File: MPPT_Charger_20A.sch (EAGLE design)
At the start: 113 parts, among them IC1 LM358D, Q1 IRFR3607, Q2 IRFR3607, Q3 IRFR3607, Q5 IRFR3607, Q7 ZXMP10A13FTA, T1 MMBT3904, U1 SN65HVD230, U2 INA199A1DCKR, U3 LM5101A, U4 MCP16311, U5 MIC5225, U6 STM32F072CB, U7 INA199A1DCKR, Y1 8MHz

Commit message: Updated revision with 20A charge current
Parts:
- removed BATTERY: MKDS_5/2-9,52, resolut:MKDS_5/2-9,52
- removed H1, H2, H3, H4: MOUNT-HOLE2.8, holes:MOUNT-HOLE2.8
- removed IC1: LM358D, linear:LM358D
- removed K1: (no value), Input-Output_Connectors_rev15d:629105150521
- removed LED3: (no value), SparkFun-LED:LED3MM
- removed LED4, LED5, LED6: (no value), SparkFun-LED:LED0603
- removed Q5: IRFR3607, LibreSolar:MOSFET_N_DPAK
- removed Q7: ZXMP10A13FTA, transistor-small-signal:BSS84
- removed R48: 2.2k, rcl:R-EU_R0603
- removed S2: (no value), LibreSolar:SWITCH-DPDT_CK_JS
- removed SWD: CORTEX_DEBUGSMD, LibreSolar:CORTEX_DEBUGSMD
- removed X1: (no value), crystal:CRYSTALMM20SS
- added BAT: MKDS_5/2-9,52, resolut:MKDS_5/2-9,52
- added C33, C36: 2.2µ, LibreSolar:CAPACITOR_0603
- added C34: 100n, LibreSolar:CAPACITOR_0603
- added C35: 1µ, LibreSolar:CAPACITOR_0603
- added C37: 10µ, rcl:C-EUC0805
- added C38: 100p, LibreSolar:CAPACITOR_0603
- added C39: DNP, LibreSolar:CAPACITOR_0603
- added D11: 1N4148W-7-F, SparkFun-DiscreteSemi:DIODESOD123
- added D12: SS16FP, resolut:SCHOTTKY-DIODEPOWERDI123
- added D6, D8: (no value), SparkFun-LED:LED0603
- added I2C: (no value), SparkFun-Connectors:M04PTH
- added IC2: LM4040CYM3-2.5, texas:LM4041A12DBZ
- added JP3: RJ45, SparkFun-Connectors:RJ45-8PTH
- added NTC1, NTC2: NTC10k, LibreSolar:THERMISTOR_0603
- added Q4: CSD18540Q5B, LibreSolar:MOSFET_N_5X6
- added R34: 100k, LibreSolar:RESISTOR_R0603
- added R35, R36, R41: 2.2k, LibreSolar:RESISTOR_R0603
- added R37: 10k, LibreSolar:RESISTOR_R0603
- added R39, R40: 1M, LibreSolar:RESISTOR_R0603
- added R42, R43: 330, LibreSolar:RESISTOR_R0603
- added RESET: (no value), EAGLE-TACT_SWITCHES-rev16e:430182050816
- added T2: MMBT3904, transistor:MMBT3904LT1-NPN-SOT23-BEC
- added U$1: LIBRESOLAR_LOGO, LibreSolar:LIBRESOLAR_LOGO
- added USB: USB_MICRO_B, LibreSolar:USB_MICRO_B
- added Y2: ABS25-32.768KHZ-T, crystal:CRYSTALMM20SS
- C1: value 470µ -> 1000µ; device rcl:CPOL-EUE5-13 -> rcl:CPOL-EUE7.5-16; MPN EEUFR1J471B -> EEUFC1J102; OC_FARNELL 2079308 -> 9692576
- C10: value 4.7µ -> 100n; device rcl:C-EUC1210 -> LibreSolar:CAPACITOR_0603; MPN GRM31CR71H475KA12L -> GRM188R71H104KA93D; OC_FARNELL 1735545 -> 8820023
- C11: value 22µ -> 100n; device rcl:C-EUC1210 -> LibreSolar:CAPACITOR_0603; MF MULTICOMP -> MURATA; MPN MC1210B226M160CT -> GRM188R71H104KA93D; OC_FARNELL 2320948 -> 8820023
- C12, C23: value 100n -> 1µ; device rcl:C-EUC0603 -> LibreSolar:CAPACITOR_0603; MF MURATA -> AVX; MPN GRM188R71H104KA93D -> 08055C104KAT2A; OC_FARNELL 8820023 -> 499687
- C13: value 0 -> 100n; device rcl:C-EUC0603 -> LibreSolar:CAPACITOR_0603; MF AVX -> MURATA; MPN 08055C104KAT2A -> GRM188R71H104KA93D; OC_FARNELL 499687 -> 8820023
- C14, C15: value 100n -> 10µ; device rcl:C-EUC0603 -> rcl:C-EUC0805; MPN GRM188R71H104KA93D -> GRM21BR61E106KA73L; OC_FARNELL 8820023 -> 1735530
- C16, C17, C19, C26, C30: device rcl:C-EUC0603 -> LibreSolar:CAPACITOR_0603
- C18: value 470µ -> 100n; device rcl:CPOL-EUE5-13 -> LibreSolar:CAPACITOR_0603; MF PANASONIC ELECTRONIC COMPONENTS -> MURATA; MPN EEUFR1J471B -> GRM188R71H104KA93D; OC_FARNELL 2079308 -> 8820023
- C2: value 1µ -> 1000µ; device rcl:C-EUC0805 -> rcl:CPOL-EUE7.5-16; MF TDK -> PANASONIC ELECTRONIC COMPONENTS; MPN C2012X7S2A105M125AB -> EEUFC1J102; OC_FARNELL 2528783 -> 9692576
- C20: value 100n -> 1µ; device rcl:C-EUC0603 -> rcl:C-EUC0805; MF MURATA -> (none); MPN GRM188R71H104KA93D -> (none); OC_FARNELL 8820023 -> unknown
- C21: value 100n -> 4.7µ; device rcl:C-EUC0603 -> rcl:C-EUC1210; MPN GRM188R71H104KA93D -> GRM31CR71H475KA12L; OC_FARNELL 8820023 -> 1735545
- C22: value 100n -> 10µ; device rcl:C-EUC0603 -> rcl:C-EUC0805; MF AVX -> MURATA; MPN 06035C104KAT2A -> GRM21BR61E106KA73L; OC_FARNELL 1301804 -> 1735530
- C24: value 100n -> 2.2µ; device rcl:C-EUC0603 -> LibreSolar:CAPACITOR_0603; MF MURATA -> AVX; MPN GRM188R71H104KA93D -> 0805YC475KAT2A; OC_FARNELL 8820023 -> 1657937
- C25: value 2.2µ -> 100n; device rcl:C-EUC0603 -> LibreSolar:CAPACITOR_0603; MF AVX -> MURATA; MPN 0805YC475KAT2A -> GRM188R71H104KA93D; OC_FARNELL 1657937 -> 8820023
- C27: value 2.2µ -> 12.5p; device rcl:C-EUC0603 -> LibreSolar:CAPACITOR_0603; MF AVX -> MURATA; MPN 0805YC475KAT2A -> GRM188R71H104KA93D; OC_FARNELL 1657937 -> 8820023
- C28: value 270µ -> 12.5p; device rcl:CPOL-EUE5-10.5 -> LibreSolar:CAPACITOR_0603; MF PANASONIC ELECTRONIC COMPONENTS -> MURATA; MPN EEUFR1J271LB -> GRM188R71H104KA93D; OC_FARNELL 2079304 -> 8820023
- C29, C9: value 1µ -> 100n; device rcl:C-EUC0603 -> LibreSolar:CAPACITOR_0603; MF AVX -> MURATA; MPN 08055C104KAT2A -> GRM188R71H104KA93D; OC_FARNELL 499687 -> 8820023
- C3: value 1µ -> 2.2µ; device rcl:C-EUC0805 -> rcl:C-EUC1210; MF TDK -> (none); MPN C2012X7S2A105M125AB -> (none); OC_FARNELL 2528783 -> unknown
- C31, C32: value 12.5p -> 100n; device rcl:C-EUC0603 -> LibreSolar:CAPACITOR_0603
- C4: value 680µ -> 1µ; device rcl:CPOL-EUE5-10.5 -> LibreSolar:CAPACITOR_0805; MF PANASONIC ELECTRONIC COMPONENTS -> (none); MPN EEUFR1V681LB -> (none); OC_FARNELL 1800669 -> unknown
- C5: value 100n -> 1µ; device rcl:C-EUC0603 -> LibreSolar:CAPACITOR_0805; MF MURATA -> (none); MPN GRM188R71H104KA93D -> (none); OC_FARNELL 8820023 -> unknown
- C6: value 1µ -> 1n; device rcl:C-EUC0603 -> rcl:C-EUC0805; MF AVX -> MULTICOMP; MPN 08055C104KAT2A -> MCU0805C102JCT; OC_FARNELL 499687 -> 9406212
- C7: value 1n -> 680µ; device rcl:C-EUC0805 -> rcl:CPOL-EUE5-10.5; MF MULTICOMP -> PANASONIC ELECTRONIC COMPONENTS; MPN MCU0805C102JCT -> EEUFR1V681LB; OC_FARNELL 9406212 -> 1800669
- C8: value 100n -> 680µ; device rcl:C-EUC0603 -> rcl:CPOL-EUE5-10.5; MF MURATA -> PANASONIC ELECTRONIC COMPONENTS; MPN GRM188R71H104KA93D -> EEUFR1V681LB; OC_FARNELL 8820023 -> 1800669
- D2: value 1N4148W-7-F -> SS16FP; device SparkFun-DiscreteSemi:DIODESOD123 -> resolut:SCHOTTKY-DIODEPOWERDI123; MF MULTICOMP -> DIODES INC.; MPN 1N4148W -> DFLS1100-7; OC_FARNELL 1621821 -> 1713889
- D3: value PESD2CAN -> NUP2105L
- D4: value 1N4148W-7-F -> (none); device SparkFun-DiscreteSemi:DIODESOD123 -> LibreSolar:USBLC6-2; MF MULTICOMP -> (none); MPN 1N4148W -> (none); OC_FARNELL 1621821 -> (none)
- F1: value 12A -> 25A; device LibreSolar:FUSE_BLADE_STD -> LibreSolar:FUSE_KEYSTONE-3557-2; MPN 3522-2 -> 3557-2; OC_FARNELL 1608220 -> 2292904
- JP1: value RJ45 -> CORTEX_DEBUGSMD; device SparkFun-Connectors:RJ45-8PTH -> LibreSolar:CORTEX_DEBUGSMD; MF AMPHENOL COMMERCIAL PRODUCTS -> (none); MPN RJHSE-5080 -> (none); OC_FARNELL 1860577 -> unknown
- JP4, UEXT: OC_FARNELL (none) -> unknown
- L1: device PowerMagnetics:WE-HCF_2818_7443643300 -> LibreSolar:L-FERYSTER-DTMSS-27/0,033/20-H; MF COILCRAFT -> (none); MPN SER2918H-223KL -> (none); OC_FARNELL 2288918 -> unknown
- L2: value 47µH -> 4.7uH; device PowerMagnetics:WE-TPC_4818/4828 -> rcl:L-EUL2012C; MPN 744043470 -> 74476404; OC_FARNELL 1890607 -> 2471630
- L3: value 22µ -> 22µH; device LibreSolar:L-BOURNS2300-H -> PowerMagnetics:WE-TPC_4818/4828; MF BOURNS -> WURTH ELEKTRONIK; MPN 2305-V-RC -> 744043470; OC_FARNELL 1929755 -> 1890607
- L4: value WE-SD_744710215 -> (none); device PowerMagnetics:WE-SD_744710215 -> EAGLE-EMC_COMPONENTS-rev16f:WE-CBA_0603(WB/HS); MF WURTH ELEKTRONIK -> (none); MPN 744710215 -> (none); OC_FARNELL 1635814 -> unknown
- LOAD, SOLAR: MF (none) -> PHOENIX CONTACT; MPN (none) -> 1714971; OC_FARNELL unknown -> 3704701
- Q1, Q2, Q3: value IRFR3607 -> CSD18540Q5B; device LibreSolar:MOSFET_N_DPAK -> LibreSolar:MOSFET_N_5X6; MF INTERNATIONAL RECTIFIER -> TEXAS INSTRUMENTS; MPN IRFR3607TRPBF -> CSD18540Q5BT; OC_FARNELL 2101420 -> 2447870
- R1, R3: value 4.7 -> 3.3; device rcl:R-EU_R0805 -> LibreSolar:RESISTOR_R0805
- R10: value 120k -> 3.3; device rcl:R-EU_R0603 -> LibreSolar:RESISTOR_R0805; MF YAGEO (PHYCOMP) -> BOURNS; MPN RC0603FR-07120KL -> CR0805-FX-1001ELF; OC_FARNELL 9238735 -> 2008380
- R11: value 10k -> 1k; device rcl:R-EU_R0603 -> LibreSolar:RESISTOR_R0603; MPN RC0603FR-0710KL -> RC0603FR-071KL.; OC_FARNELL 9238603 -> 9238484
- R12: value 150k -> 2.2k; device rcl:R-EU_R0603 -> LibreSolar:RESISTOR_R0603; MPN RC0603FR-07150KL -> RC0603FR-071KL.; OC_FARNELL 9238743 -> 9238484
- R13: value 6.8k -> 2.2k; device rcl:R-EU_R0603 -> LibreSolar:RESISTOR_R0603; MPN RC0603FR-076K8L -> RC0603FR-071KL.; OC_FARNELL 9238581 -> 9238484
- R14: value 4.7 -> 150k; device rcl:R-EU_R1206 -> LibreSolar:RESISTOR_R0603; MPN RC1206FR-074R7L -> RC0603FR-071KL.; OC_FARNELL 9236600 -> 9238484
- R15: value 330 -> 150k; device rcl:R-EU_R0603 -> LibreSolar:RESISTOR_R0603; MPN RC0603FR-07330RL -> RC0603FR-071KL.; OC_FARNELL 9238425 -> 9238484
- R16, R29, R30: value 1k -> 10k; device rcl:R-EU_R0603 -> LibreSolar:RESISTOR_R0603; MPN RC0603FR-071KL. -> RC0603FR-0710KL; OC_FARNELL 9238484 -> 9238603
- R17: value 1k -> 2m; device rcl:R-EU_R0603 -> rcl:R-EU_R2512; MF YAGEO (PHYCOMP) -> BOURNS; MPN RC0603FR-071KL. -> CRF2512-FX-R005ELF; OC_FARNELL 9238484 -> 2008327
- R18, R19: value 10k -> 2.2k; device rcl:R-EU_R0603 -> LibreSolar:RESISTOR_R0603; MPN RC0603FR-0710KL -> RC0603FR-071KL.; OC_FARNELL 9238603 -> 9238484
- R2: value 4.7 -> 1M; device rcl:R-EU_R0805 -> LibreSolar:RESISTOR_R0603; MF BOURNS -> YAGEO (PHYCOMP); MPN CR0805-FX-1001ELF -> RC0603FR-071ML; OC_FARNELL 2008380 -> 9238840
- R20: value 33k -> 1k; device rcl:R-EU_R0603 -> LibreSolar:RESISTOR_R0603; MPN RC0603FR-0733KL -> RC0603FR-071KL.; OC_FARNELL 9238662 -> 9238484
- R21: value 10k -> 150k; device rcl:R-EU_R0603 -> LibreSolar:RESISTOR_R0603; MPN RC0603FR-0710KL -> RC0603FR-071KL.; OC_FARNELL 9238603 -> 9238484
- R22: value 2.2k -> 150k; device rcl:R-EU_R0603 -> LibreSolar:RESISTOR_R0603; MPN RC0603FR-072K2L. -> RC0603FR-071KL.; OC_FARNELL 9238522 -> 9238484
- R23: value 2.2k -> 10k; MPN RC0603FR-072K2L. -> RC0603FR-0710KL; OC_FARNELL 9238522 -> 9238603
- R24: value 330 -> 100k; device rcl:R-EU_R0603 -> LibreSolar:RESISTOR_R0603; MPN RC0603FR-07330RL -> RC0603FR-07150KL; OC_FARNELL 9238425 -> 9238743
- R25: value 120 -> 100k; device rcl:R-EU_R1206 -> LibreSolar:RESISTOR_R0603; MF WELWYN -> YAGEO (PHYCOMP); MPN WCR0805-120RFI -> RC0603FR-071KL.; OC_FARNELL 1100308 -> 9238484
- R26: value 0R -> 5.6k; device rcl:R-EU_R0603 -> LibreSolar:RESISTOR_R0603; MF PANASONIC ELECTRONIC COMPONENTS -> YAGEO (PHYCOMP); MPN ERJ3GEY0R00V -> RC0603FR-076K8L; OC_FARNELL 2059527 -> 9238581
- R27: device rcl:R-EU_R0603 -> LibreSolar:RESISTOR_R0603
- R28: value 0R -> 52.3k; device rcl:R-EU_R0603 -> LibreSolar:RESISTOR_R0603; MF PANASONIC ELECTRONIC COMPONENTS -> BOURNS; MPN ERJ3GEY0R00V -> CR0805-FX-1001ELF; OC_FARNELL 2059527 -> 2008380
- R31: value 100k -> 120; device rcl:R-EU_R0603 -> LibreSolar:RESISTOR_R1206; MF YAGEO (PHYCOMP) -> WELWYN; MPN RC0603FR-0710KL -> WCR0805-120RFI; OC_FARNELL 9238603 -> 1100308
- R32: value 10k -> 0; device rcl:R-EU_R0603 -> LibreSolar:RESISTOR_R0603
- R33: value 330 -> 0; device rcl:R-EU_R0603 -> LibreSolar:RESISTOR_R0603; MPN RC0603FR-07330RL -> RC0603FR-0710KL; OC_FARNELL 9238425 -> 9238603
- R4: device rcl:R-EU_R1206 -> LibreSolar:RESISTOR_R1206
- R45: value 2.2k -> 56k; device rcl:R-EU_R0603 -> LibreSolar:RESISTOR_R0603; MF YAGEO (PHYCOMP) -> BOURNS; MPN RC0603FR-072K2L. -> CR0805-FX-1001ELF; OC_FARNELL 9238522 -> 2008380
- R5: value 120k -> 4.7; device rcl:R-EU_R0603 -> LibreSolar:RESISTOR_R1206; MPN RC0603FR-07120KL -> RC1206FR-074R7L; OC_FARNELL 9238735 -> 9236600
- R6: value 10k -> 2m; device rcl:R-EU_R0603 -> rcl:R-EU_R2512; MF YAGEO (PHYCOMP) -> BOURNS; MPN RC0603FR-0710KL -> CRF2512-FX-R005ELF; OC_FARNELL 9238603 -> 2008327
- R7: value 1M -> 2.2k; device rcl:R-EU_R0603 -> LibreSolar:RESISTOR_R0603; MPN RC0603FR-071ML -> RC0603FR-071KL.; OC_FARNELL 9238840 -> 9238484
- R8: value 5m -> 2.2k; device rcl:R-EU_R2512 -> LibreSolar:RESISTOR_R0603; MF BOURNS -> YAGEO (PHYCOMP); MPN CRF2512-FX-R005ELF -> RC0603FR-071KL.; OC_FARNELL 2008327 -> 9238484
- R9: value 5m -> 33k; device rcl:R-EU_R2512 -> LibreSolar:RESISTOR_R0603; MF BOURNS -> YAGEO (PHYCOMP); MPN CRF2512-FX-R005ELF -> RC0603FR-0733KL; OC_FARNELL 2008327 -> 9238662
- U1: value SN65HVD230 -> LM5107; device LibreSolar:SN65HVD230 -> LibreSolar:LM5107; MPN SN65HVD230DR -> LM5107MA; OC_FARNELL 8452148 -> 1008269
- U2: value INA199A1DCKR -> LM2665; device Texas Instruments_By_element14_Batch_1:INA199A1DCKR -> LibreSolar:LM2665_; MF (none) -> TEXAS INSTRUMENTS; MPN (none) -> LM2665M6/NOPB; OC_FARNELL (none) -> 1469163
- U3: value LM5101A -> MCP16331-CH; device LibreSolar:LM5101A -> LibreSolar:MCP16331-CH; MF TEXAS INSTRUMENTS -> MICROCHIP; MPN LM5101AM/NOPB -> MCP16331T-E/CH; OC_FARNELL 1559514 -> 2448515
- U4: value MCP16311 -> AP2210-3.3; device LibreSolar:MCP16311 -> LibreSolar:AP2210-3.3V; MPN MCP16311-E/MS -> MIC5225-3.3YM5-TR; OC_FARNELL 2414134 -> 2510262
- U5: value MIC5225 -> TJA1042T/3; device SparkFun-PowerIC:V_REG_MIC5235 -> LibreSolar:TJA1042T/3; MF MICROCHIP -> NXP; MPN MIC5225-3.3YM5-TR -> TJA1042T/3/1J; OC_FARNELL 2510262 -> 2574957
- U6: MF (none) -> STMICROELECTRONICS
- U7: value INA199A1DCKR -> LM358A; device Texas Instruments_By_element14_Batch_1:INA199A1DCKR -> LibreSolar:OPAMP_SO8; MF (none) -> TEXAS INSTRUMENTS; MPN (none) -> LM358ADR; OC_FARNELL (none) -> 7527007
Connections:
- removed net FUSE+: BATTERY-1.KL, F1.1A, F1.1B
- removed net LC_OUT: C13.2, L4.2, Q3.S, R7.1
- removed net LED3: R33.2, U6.PB12
- removed net LOAD_EN: R23.1, U6.PB2
- removed net N$1: R1.1, U3.HB
- removed net N$32: U6.PB1
- removed net N$34: U6.PB0
- removed net N$35: LED3.A, LED6.A, R33.1
- removed net N$37: K1.1VCC
- removed net N$49: U6.PB14
- removed net N$51: U6.PA15
- removed net SOLAR+: C28.+, L4.1, SOLAR-2.KL
- removed net VREF: IC1A.-IN, IC1A.OUT, U2.REF, U7.REF
- new net !LOAD_EN!: R13.1, U6.PB2
- new net +5V: C22.1, C23.1, C26.1, C35.1, C37.1, C9.1, D11.A, D12.A, L3.2, R28.2, U2.V+, U4.EN, U4.IN, U5.VCC, U7P.V+
- new net BOOT0: C36.1, R39.1, R41.2, U6.BOOT0
- new net CAN_STB: U5.STB, U6.PA15
- new net DCDC_OUT: C20.1, C7.+, C8.+, F1.2A, F1.2B, L1.2, L2.2, LOAD-1.KL, R25.2
- new net HB: R10.1, U1.HB
- new net I2C2_SCL: I2C.4, U6.PB10
- new net I2C2_SDA: I2C.3, U6.PB11
- new net N$23: R18.1, R22.1, U7B.-IN
- new net N$36: R11.1, R15.2, U7A.OUT
- new net N$40: JP4.1, R31.2
- new net N$99: R15.1, R7.1, U7A.-IN
- new net REF_I_DCDC: R21.1, U6.PA4
- new net SOLAR-: C5.2, Q2.D, SOLAR-2.KL
- new net TEMP: C16.1, NTC1.1, NTC2.1, R23.1, U6.PA1
- new net USART1_RX: JP1.NC/TDI, U6.PA10
- new net USART1_TX: JP1.SWO/TDO, U6.PA9
- new net VDDA: C34.1, L4.1, U6.VDDA
- new net V_REF: IC2.C, R37.1, U6.PA5
- net !RESET: now also C29.1, JP1.NRESET, R40.1, R45.1, RESET.1, RESET.3; no longer C23.1, SWD.NRESET
- net +10V: now also C12.1, C14.1, D12.C, R9.1, U1.VDD, U2.OUT; no longer C11.1, C29.1, C6.1, D4.A, L2.2, R20.2, R5.2, U3.VDD, U5.EN, U5.IN
- net +3V3: now also C31.1, C32.1, C33.1, I2C.2, JP1.VCC, L4.2, R23.2, R35.2, R36.2, R37.2, R39.2, R40.2, U4.OUT, U5.VIO; no longer C17.1, C19.1, C20.1, C21.1, C22.1, C26.1, C27.1, IC1P.V+, JP4.2, R29.2, R45.2, R48.2, SWD.VCC, U1.VDD, U2.V+, U5.OUT, U6.VDDA, U7.V+
- net BAT+: now also BAT-1.KL, F1.1A, F1.1B; no longer C10.1, C4.+, F1.2A, F1.2B, L1.2, L3.1, LOAD-2.KL, R10.2, U4.EN, U4.VIN
- net BAT-: now also BAT-2.KL, R17.1, R19.2, R6.2, R7.2; no longer BATTERY-2.KL, R8.2, R9.1, U2.IN+, U7.IN-
- net BAT-1: now also Q4.S, R16.1, R17.2, R8.2; no longer Q5.S, R21.1, R9.2, U7.IN+
- net CAN_GND: now also JP3.3, JP3.7; no longer JP1.3, JP1.7, R28.2
- net CAN_H: now also JP3.1, R31.1, U5.CANH; no longer JP1.1, S2.3, U1.CANH
- net CAN_L: now also JP3.2, JP4.2, U5.CANL; no longer JP1.2, R25.1, U1.CANL
- net CAN_RX: now also U5.RXD; no longer U1.R
- net CAN_SHLD: now also JP3.6; no longer JP1.6
- net CAN_TX: now also U5.TXD; no longer U1.D
- net CAN_V+: now also JP3.8; no longer D4.C, JP1.8
- net DCDC_IN: now also C2.+, C4.1, C5.1, R24.2, SOLAR-1.KL; no longer C18.+, C2.1, D2.A, Q3.D, Q7.G, R12.2
- net GND: now also C13.2, C18.2, C2.-, C28.2, C33.2, C34.2, C35.2, C36.2, C37.2, C38.2, C39.2, C4.2, C7.-, C8.-, D2.A, D4.GND, D6.C, D8.C, I2C.1, IC2.A, JP1.GND@3, JP1.GND@5, NTC1.2, NTC2.2, Q3.S, R18.2, R2.2, R26.1, R27.1, R29.1, R34.1, R5.1, RESET.2, RESET.4, T2.E, U2.SD, U3.GND, U4.GND, U7P.V-, USB.GND; no longer C10.2, C15.2, C18.-, C19.2, C2.2, C28.-, C4.-, C6.2, IC1P.V-, K1.5GND, K1.GND@1, K1.GND@2, LED3.C, LED4.C, LED5.C, LED6.C, R11.1, R13.1, R26.2, R28.1, R30.1, R31.1, R32.1, R8.1, SOLAR-1.KL, SWD.GND@3, SWD.GND@5, U2.IN-, U3.VSS, U4.AGND, U4.PGND, U7.GND
- net HS_DRV: now also R1.1, U1.HO; no longer R2.1, U3.HO
- net I2C1_SCL: now also R36.1; no longer R48.1
- net I2C1_SDA: now also R35.1; no longer R45.1
- net I_DCDC: now also C13.1, R20.2, U6.PB1; no longer C15.1, R16.2, U6.PA7
- net I_LOAD: now also C11.1, R11.2, U6.PB0; no longer C14.1, R17.2, U6.PA6
- net LED1: now also R42.2, U6.PB14; no longer R15.2, U6.PA9
- net LED2: now also R43.2, U6.PB15; no longer R24.2, U6.PA10
- net LOAD-: now also LOAD-2.KL, Q4.D; no longer LOAD-1.KL, Q5.D
- net LOAD_G: now also Q4.G, R12.2; no longer Q5.G, R22.2
- net LS_DRV: now also U1.LO; no longer U3.LO
- net N$10: now also D4.I/O2-1, USB.D+; no longer D1.C, D2.C, Q7.S
- net N$11: now also R12.1, R9.2; no longer R20.1, R22.1
- net N$12: now also C6.2, R5.2; no longer C7.2, R14.2
- net N$13: now also C15.1, U2.CAP+; no longer C8.2, L2.1, U4.SW
- net N$14: now also C15.2, U2.CAP-; no longer C8.1, U4.BOOST
- net N$15: now also C27.1, R30.2, Y2.1; no longer C31.1, R27.2, X1.1
- net N$16: now also R28.1, R29.2, U3.V_FB; no longer C9.1, U4.VCC
- net N$17: now also C28.1, Y2.2; no longer C32.1, X1.2
- net N$18: now also R19.1, R21.2, U7B.+IN; no longer R16.1, U2.OUT
- net N$19: now also R14.2, R8.1, U7A.+IN; no longer IC1A.+IN, IC1B.+IN, R29.1, R30.2
- net N$2: now also C10.1, R10.2; no longer C5.1, R1.2
- net N$20: now also Q1.G, R1.2; no longer R17.1, U7.OUT
- net N$21: now also R41.1, T2.C; no longer U6.PB15
- net N$22: now also C19.1, D11.C, U3.BOOST; no longer R5.1, R6.2, U4.VFB
- net N$24: now also R13.2, R16.2; no longer R21.2, R23.2
- net N$25: now also C19.2, D2.C, L3.1, U3.SW; no longer U6.PB10
- net N$26: now also C21.1, L2.1, U3.EN, U3.V_IN; no longer U6.PB11
- net N$27: now also D4.I/O1-1, USB.D-; no longer K1.2D-, R18.2
- net N$28: now also C38.1, U4.BP; no longer K1.3D+, R19.2
- net N$29: now also R34.2, USB.ID; no longer K1.4ID, R31.2
- net N$3: now also D4.I/O1, R32.2; no longer R26.1, U1.RS
- net N$30: now also C39.1, USB.SHLD; no longer JP4.1, R32.2, U6.BOOT0
- net N$4: now also D1.C, Q2.G, R2.1; no longer D1.A, Q1.G, R2.2
- net N$43: now also D6.A, R42.1; no longer LED4.A, R15.1
- net N$46: now also D8.A, R43.1; no longer LED5.A, R24.1
- net N$5: now also R45.2, T2.B; no longer R25.2, S2.2
- net N$6: now also R20.1, R22.2, U7B.OUT; no longer IC1B.-IN, IC1B.OUT
- net N$7: now also R30.1; no longer R27.1
- net N$8: now also D4.I/O2, R33.2; no longer C13.1, Q3.G, Q7.D, R7.2
- net N$9: now also D1.A, Q3.G; no longer Q2.G
- net SSEL: now also U6.PA0-WKUP; no longer U6.PA1
- net SWCLK: now also JP1.SWDCLK/TCK; no longer SWD.SWDCLK/TCK
- net SWDIO: now also JP1.SWDIO/TMS; no longer SWD.SWDIO/TMS
- net SW_NODE: now also C10.2, C6.1, Q3.D, U1.HS; no longer C5.2, C7.1, L3.2, Q2.D, U3.HS
- net TIM1_CH1: now also U1.LI; no longer U3.HI
- net TIM1_CH1N: now also U1.HI; no longer U3.LI
- net USB_DM: now also R32.1; no longer R18.1
- net USB_DP: now also R33.1; no longer R19.1
- net V_BAT: now also C18.1, R25.1, R27.2, U6.PA6; no longer C12.1, R10.1, R11.2, U6.PA4
- net V_SOLAR: now also C17.1, R24.1, R26.2, U6.PA7; no longer C16.1, R12.1, R13.2, U6.PA5
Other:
- note added: "(or DFLS160-7)"
- note added: "10 V"
- note added: "1000µ, 35V, 2.6A Panasonic EEUFR1V102"
- note added: "1000µF, 63V, 2.73A, 16x25 United Chemi EKYB630ELL102ML25S"
- note added: "1µ, 100V, X7S TDK C2012X7S2A105M125AB 2.2µ, 100V, X7R Murata GRM31CR72A225KA73L"
- note added: "5 V"
- note added: "Alt. to USBLC6-2: WE-TVS 82400102"
- note added: "Alternative: 330R at MOSFET gate --> 10.4/330 = 31 mA max"
- note added: "Alternative: PESD2CAN"
- note added: "C_in: TDK C3225X7R2A225K230AB C_out: Murata GRM21BR60J226ME39L"
- note added: "DCDC current"
- note added: "Design: Martin Jäger http://libre.solar License: CC-BY-SA"
- note added: "Diff. amp. reference defined by DAC pin instead of GND: variable zero current set point"
- note added: "Display connector"
- note added: "If not stated otherwise, all MLCC 50V X7R"
- note added: "Inductor: WE-TPC-4818 744042220 or Bourns SRR4028-220Y"
- note added: "Layout for Vin<60V, Iout<300mA, Vout=5V"
- note added: "Load output"
- note added: "Max current output: 150mA Alternative: MIC5225"
- note added: "Murata GRM21BR61E106KA73L 10µF, 25V, X5R"
- note added: "Reset & boot switch - Press long (>2s) for USB bootloader (BOOT0 cap charged) - Press short (<1s) for normal reset"
- note added: "Reset and boot circuit"
- note added: "Voltage reference"
- note added: "min. 65 uA operating current needed"
- note removed: "-100V PMOS"
- note removed: "10.4 V"
- note removed: "16V"
- note removed: "1µ, 100V, X7S TDK C2012X7S2A105M125AB"
- note removed: "470µ, 63V, 1995 mA ripple current Panasonic EEUFR1J471"
- note removed: "680µ, 35V Panasonic EEUFR1V681"
- note removed: "Alternative: NUP2105L"
- note removed: "Charge current amp"
- note removed: "Design: Martin Jäger www.libre.solar License: CC-BY-SA"
- note removed: "Inductor alternatives: - 8A: Coilcraft SER2918H-223 - 12A: Würth HCF 7443642200 - Toroid: Bourns 2305-RC"
- note removed: "Inductor: WE-TPC-4818 744042470 or Bourns SRR4028-470Y"
- note removed: "Load current amp and switch"
- note removed: "Max current output: 150mA"
- note removed: "VCC pin only 5V"
- note removed: "for MOSFET drivers"
- note removed: "for digital circuits"

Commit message: Minor changes + nice image from Aisler.net
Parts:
- BAT, SOLAR: MF PHOENIX CONTACT -> (none); MF_ALT (none) -> WURTH ELEKTRONIK; MPN 1714971 -> (none); MPN_ALT (none) -> 691250910002; OC_FARNELL 3704701 -> unknown
- C1, C2: MF PANASONIC ELECTRONIC COMPONENTS -> (none); MPN EEUFC1J102 -> EKYB630ELL102ML25S; OC_FARNELL 9692576 -> unknown
- C10, C11, C13, C16, C17, C18, C19, C25, C26, C29, C30, C31, C32, C34, C38, C39, C9: MF MURATA -> (none); MPN GRM188R71H104KA93D -> (none); OC_FARNELL 8820023 -> unknown
- C12, C23, C35: MF AVX -> (none); MPN 08055C104KAT2A -> (none); OC_FARNELL 499687 -> unknown
- C27, C28: value 12.5p -> 4.3p; MF MURATA -> (none); MPN GRM188R71H104KA93D -> (none); OC_FARNELL 8820023 -> unknown
- C6: MF MULTICOMP -> (none); MPN MCU0805C102JCT -> (none); OC_FARNELL 9406212 -> unknown
- C7, C8: value 680µ -> 820µ; MF PANASONIC ELECTRONIC COMPONENTS -> (none); MPN EEUFR1V681LB -> (none); OC_FARNELL 1800669 -> unknown
- D3: MF NXP -> ON SEMICONDUCTOR; MPN PESD2CAN -> NUP2105LT1G; OC_FARNELL 1510712 -> 2101833
- D4: MF (none) -> WURTH ELEKTRONIK; MPN (none) -> 82400102; OC_FARNELL (none) -> 1825875
- I2C: OC_FARNELL (none) -> unknown
- IC2: MF (none) -> MICROCHIP; MPN (none) -> LM4040DYM3-2.5-TR; OC_FARNELL (none) -> 2509865
- LOAD: MF PHOENIX CONTACT -> (none); MPN 1714971 -> (none); OC_FARNELL 3704701 -> unknown
- R11, R12, R13, R14, R15, R18, R19, R20, R21, R22, R25, R34, R35, R36, R41, R7, R8: MF YAGEO (PHYCOMP) -> (none); MPN RC0603FR-071KL. -> (none); OC_FARNELL 9238484 -> unknown
- R16, R23, R27, R29, R30, R32, R33, R37: MF YAGEO (PHYCOMP) -> (none); MPN RC0603FR-0710KL -> (none); OC_FARNELL 9238603 -> unknown
- R17, R6: MPN CRF2512-FX-R005ELF -> CRE2512-FZ-R002E-3; OC_FARNELL 2008327 -> (none)
- R2, R39, R40: MF YAGEO (PHYCOMP) -> (none); MPN RC0603FR-071ML -> (none); OC_FARNELL 9238840 -> unknown
- R24: MF YAGEO (PHYCOMP) -> (none); MPN RC0603FR-07150KL -> (none); OC_FARNELL 9238743 -> unknown
- R26: MF YAGEO (PHYCOMP) -> (none); MPN RC0603FR-076K8L -> (none); OC_FARNELL 9238581 -> unknown
- R31: MF WELWYN -> (none); MPN WCR0805-120RFI -> (none); OC_FARNELL 1100308 -> unknown
- R4, R5: MF YAGEO (PHYCOMP) -> (none); MPN RC1206FR-074R7L -> (none); OC_FARNELL 9236600 -> unknown
- R42, R43: MF YAGEO (PHYCOMP) -> (none); MPN RC0603FR-07330RL -> (none); OC_FARNELL 9238425 -> unknown
- R9: MF YAGEO (PHYCOMP) -> (none); MPN RC0603FR-0733KL -> (none); OC_FARNELL 9238662 -> unknown
- U1: MF TEXAS INSTRUMENTS -> (none); MPN LM5107MA -> (none); OC_FARNELL 1008269 -> unknown
- U2: MF TEXAS INSTRUMENTS -> (none); MPN LM2665M6/NOPB -> (none); OC_FARNELL 1469163 -> unknown
- U5: MF NXP -> (none); MPN TJA1042T/3/1J -> (none); OC_FARNELL 2574957 -> unknown
- U7: MF TEXAS INSTRUMENTS -> (none); MPN LM358ADR -> (none); OC_FARNELL 7527007 -> unknown
- USB: MF Amphenol FCI -> FCI; OC_FARNELL (none) -> 2506568
- Y2: value ABS25-32.768KHZ-T -> ABS25-32.768KHZ-6-T
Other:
- note added: "25V"
- note added: "820µ, 35V, 2.47A Panasonic EEU-FR1V821L"
- note removed: "1000µ, 35V, 2.6A Panasonic EEUFR1V102"

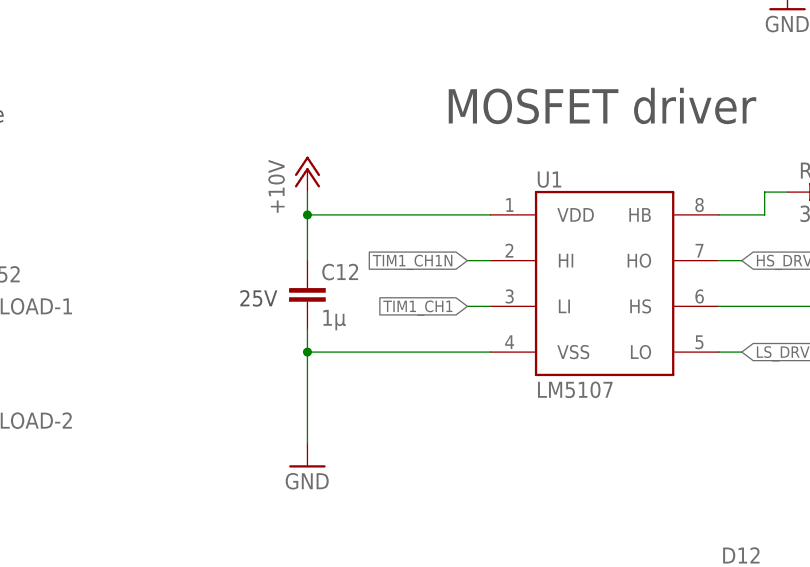
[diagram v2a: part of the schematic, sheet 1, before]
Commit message: Fixing issues #12 and #11
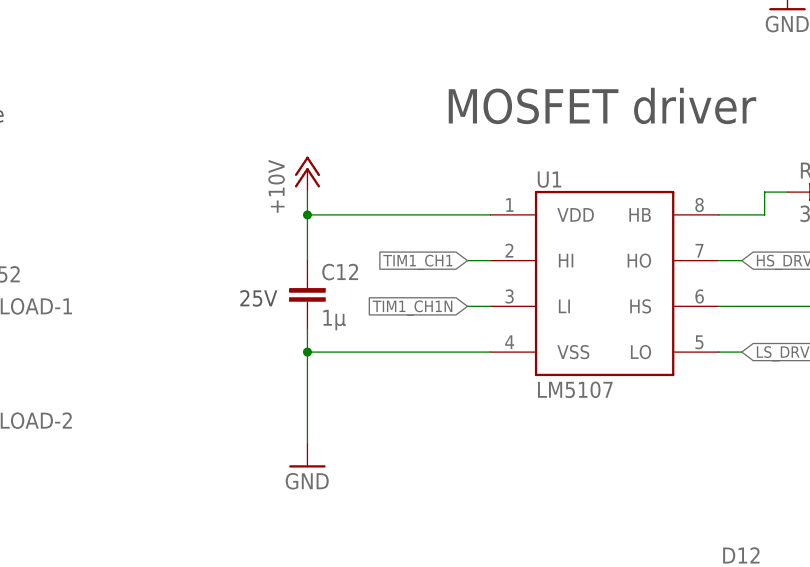
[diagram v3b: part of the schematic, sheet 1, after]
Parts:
- R23: device rcl:R-EU_R0603 -> LibreSolar:RESISTOR_R0603
- R30: value 10k -> 0
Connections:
- net TIM1_CH1: now also U1.HI; no longer U1.LI
- net TIM1_CH1N: now also U1.LI; no longer U1.HI
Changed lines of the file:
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@@
 <attribute name="OC_FARNELL" value="unknown"/>
 </part>
-<part name="R30" library="LibreSolar" deviceset="RESISTOR" device="_R0603" value="10k">
+<part name="R30" library="LibreSolar" deviceset="RESISTOR" device="_R0603" value="0">
 <attribute name="MF" value=""/>
 <attribute name="MPN" value=""/>
@@
 <part name="+3V34" library="supply1" deviceset="+3V3" device=""/>
 <part name="GND27" library="SparkFun" deviceset="GND" device=""/>
-<part name="R23" library="rcl" deviceset="R-EU_" device="R0603" value="10k">
+<part name="R23" library="LibreSolar" deviceset="RESISTOR" device="_R0603" value="10k">
 <attribute name="MF" value=""/>
 <attribute name="MPN" value=""/>
@@
 </segment>
 </net>
-<net name="TIM1_CH1N" class="0">
-<segment>
-<wire x1="170.18" y1="149.86" x2="167.64" y2="149.86" width="0.1524" layer="91"/>
-<label x="167.64" y="149.86" size="1.27" layer="95" rot="R180" xref="yes"/>
-<pinref part="U1" gate="G$1" pin="HI"/>
-</segment>
-</net>
 <net name="N$9" class="0">
 <segment>
@@
 <net name="TIM1_CH1" class="0">
 <segment>
-<label x="167.64" y="144.78" size="1.27" layer="95" rot="R180" xref="yes"/>
-<wire x1="170.18" y1="144.78" x2="167.64" y2="144.78" width="0.1524" layer="91"/>
-<pinref part="U1" gate="G$1" pin="LI"/>
+<wire x1="170.18" y1="149.86" x2="167.64" y2="149.86" width="0.1524" layer="91"/>
+<label x="167.64" y="149.86" size="1.27" layer="95" rot="R180" xref="yes"/>
+<pinref part="U1" gate="G$1" pin="HI"/>
 </segment>
 </net>
@@
 </segment>
 </net>
+<net name="TIM1_CH1N" class="0">
+<segment>
+<label x="167.64" y="144.78" size="1.27" layer="95" rot="R180" xref="yes"/>
+<wire x1="170.18" y1="144.78" x2="167.64" y2="144.78" width="0.1524" layer="91"/>
+<pinref part="U1" gate="G$1" pin="LI"/>
+</segment>
+</net>
